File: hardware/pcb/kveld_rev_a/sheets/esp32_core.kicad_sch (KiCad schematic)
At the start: 0 parts

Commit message: feat(hw): capture rev a schematic and refine enclosure
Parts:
- added C27: 1uF, Capacitor_SMD:C_0603_1608Metric, symbol Device:C
- added C28: 100nF, Capacitor_SMD:C_0603_1608Metric, symbol Device:C
- added C29: 10uF, Capacitor_SMD:C_0603_1608Metric, symbol Device:C
- added C30: 47uF, Capacitor_SMD:C_0805_2012Metric, symbol Device:C
- added R25, R26: 10k, Resistor_SMD:R_0603_1608Metric, symbol Device:R
- added U1: ESP32-S3-WROOM-1-N16 / WROOM-1U-N16, RF_Module:ESP32-S3-WROOM-1, symbol RF_Module:ESP32-S3-WROOM-1
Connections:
- new net 3V3: C28.1, C29.1, C30.1, R25.1, R26.1, U1.2 (3V3)
- new net BOOT_IO0: R26.2, U1.27 (IO0)
- new net BTN_CATEGORY: U1.4 (IO4)
- new net BTN_NEXT: U1.10 (IO17)
- new net CHG_ENABLE: U1.22 (IO14)
- new net CHG_STAT1: U1.6 (IO6)
- new net CHG_STAT2: U1.7 (IO7)
- new net CHIP_EN: C27.1, R25.2, U1.3 (EN)
- new net EPD_BUSY: U1.17 (IO9)
- new net EPD_CLK: U1.20 (IO12)
- new net EPD_CS: U1.18 (IO10)
- new net EPD_DC: U1.11 (IO18)
- new net EPD_MOSI: U1.19 (IO11)
- new net EPD_PWR_EN: U1.5 (IO5)
- new net EPD_RESET: U1.12 (IO8)
- new net FACTORY_RESET_OD: U1.31 (IO38)
- new net GND: C27.2, C28.2, C29.2, C30.2, U1.1 (GND), U1.40 (GND), U1.41 (GND)
- new net STATUS_GREEN: U1.9 (IO16)
- new net STATUS_RED: U1.8 (IO15)
- new net UART0_RX: U1.36 (RXD0)
- new net UART0_TX: U1.37 (TXD0)
- new net USB_DN: U1.13 (USB_D-)
- new net USB_DP: U1.14 (USB_D+)
- new net VBAT_SENSE: U1.39 (IO1)
- new net VBAT_SENSE_EN: U1.38 (IO2)
- new net VBUS_SENSE: U1.23 (IO21)
- no-connect marks 0 -> 13
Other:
- note added: "Preferred assembly: WROOM-1-N16. WROOM-1U-N16 stays open as the placement/RF fallback."
- title: (none) -> ESP32-S3 module core

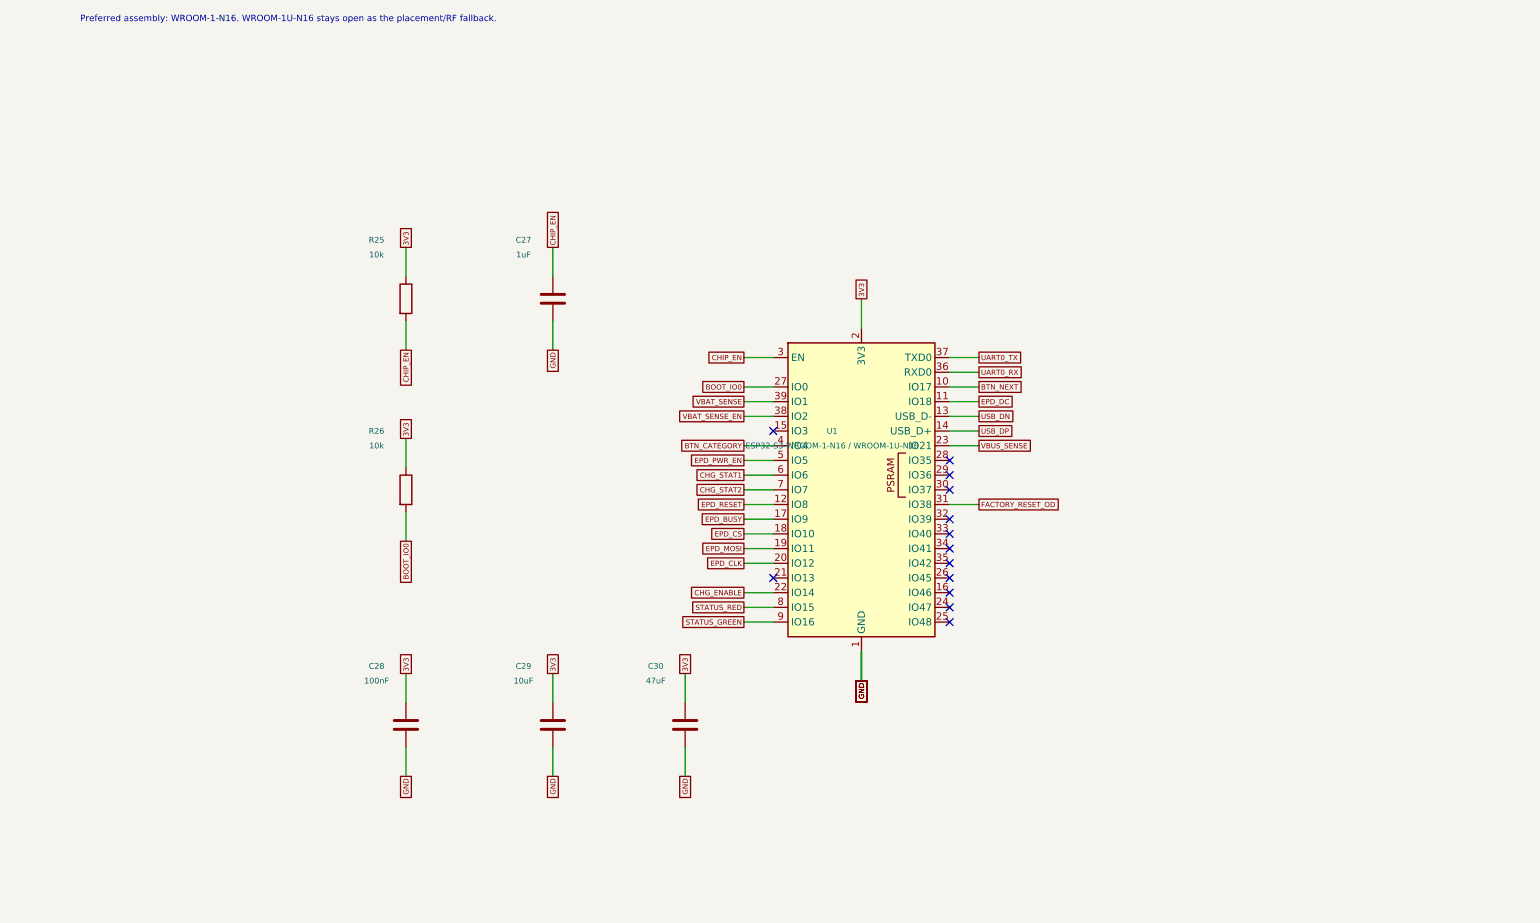
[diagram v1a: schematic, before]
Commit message: refactor(hw): consolidate and clarify schematic
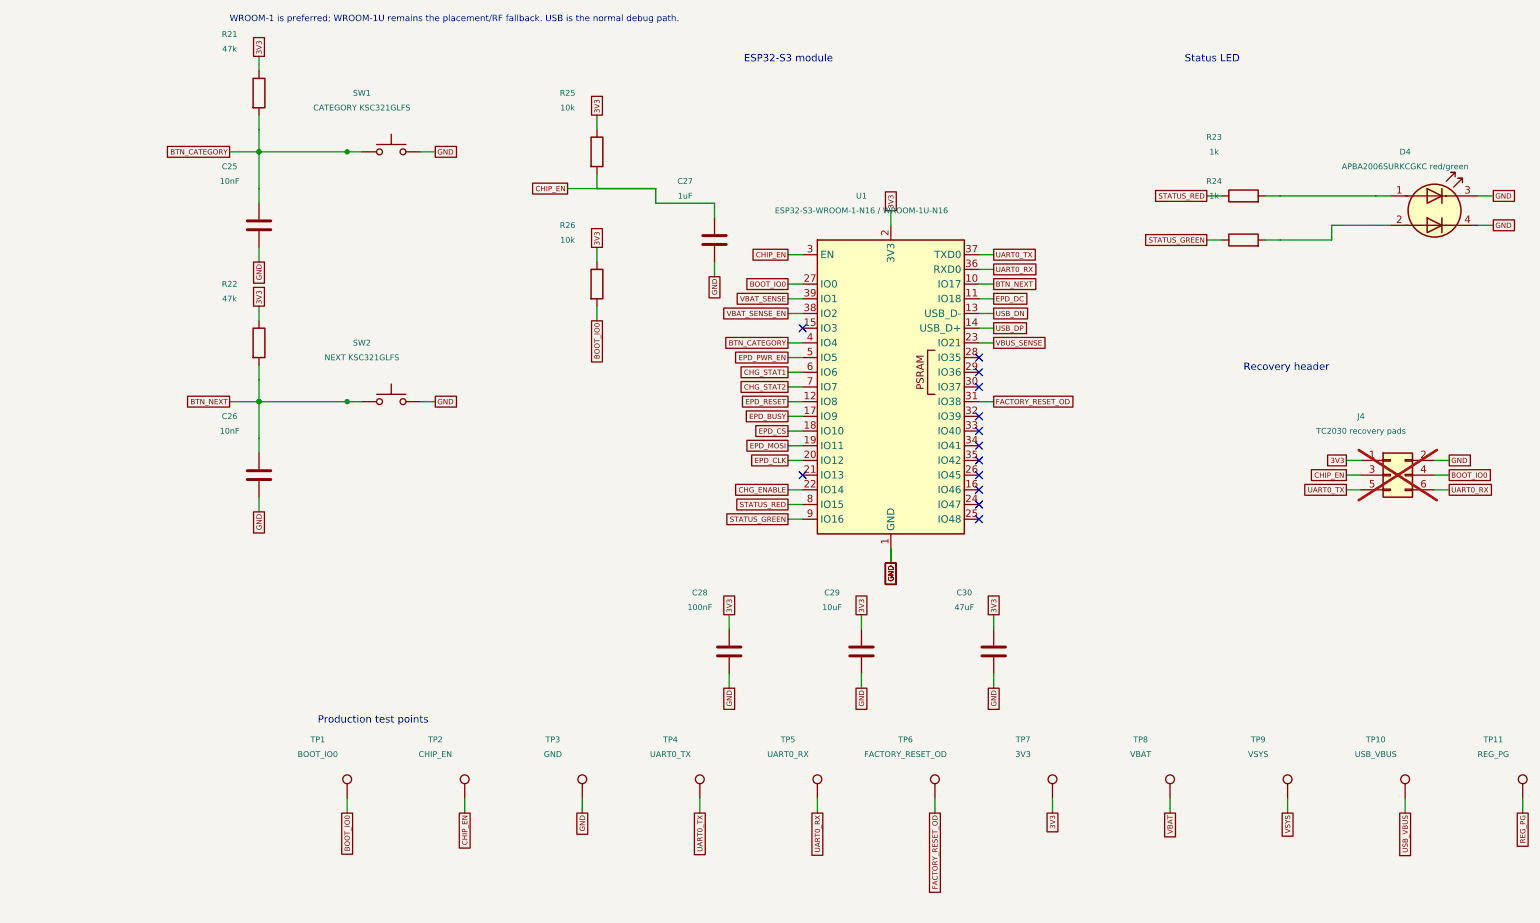
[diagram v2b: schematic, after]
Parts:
- added C25, C26: 10nF, Capacitor_SMD:C_0603_1608Metric, symbol Device:C
- added D4: APBA2006SURKCGKC red/green, symbol Device:LED_Dual_AAKK
- added J4: TC2030 recovery pads, Connector:Tag-Connect_TC2030-IDC-NL_2x03_P1.27mm_Vertical, symbol Connector_Generic:Conn_02x03_Odd_Even
- added R21, R22: 47k, Resistor_SMD:R_0603_1608Metric, symbol Device:R
- added R23, R24: 1k, Resistor_SMD:R_0603_1608Metric, symbol Device:R
- added SW1: CATEGORY KSC321GLFS, symbol Switch:SW_Push
- added SW2: NEXT KSC321GLFS, symbol Switch:SW_Push
- added TP1: BOOT_IO0, TestPoint:TestPoint_Pad_D1.0mm, symbol Connector:TestPoint
- added TP10: USB_VBUS, TestPoint:TestPoint_Pad_D1.0mm, symbol Connector:TestPoint
- added TP11: REG_PG, TestPoint:TestPoint_Pad_D1.0mm, symbol Connector:TestPoint
- added TP2: CHIP_EN, TestPoint:TestPoint_Pad_D1.0mm, symbol Connector:TestPoint
- added TP3: GND, TestPoint:TestPoint_Pad_D1.0mm, symbol Connector:TestPoint
- added TP4: UART0_TX, TestPoint:TestPoint_Pad_D1.0mm, symbol Connector:TestPoint
- added TP5: UART0_RX, TestPoint:TestPoint_Pad_D1.0mm, symbol Connector:TestPoint
- added TP6: FACTORY_RESET_OD, TestPoint:TestPoint_Pad_D1.0mm, symbol Connector:TestPoint
- added TP7: 3V3, TestPoint:TestPoint_Pad_D1.0mm, symbol Connector:TestPoint
- added TP8: VBAT, TestPoint:TestPoint_Pad_D1.0mm, symbol Connector:TestPoint
- added TP9: VSYS, TestPoint:TestPoint_Pad_D1.0mm, symbol Connector:TestPoint
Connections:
- net 3V3: now also J4.1 (Pin_1), R21.1, R22.1, TP7.1
- net BOOT_IO0: now also J4.4 (Pin_4), TP1.1
- net BTN_CATEGORY: now also C25.1, R21.2, SW1.1
- net BTN_NEXT: now also C26.1, R22.2, SW2.1
- net CHIP_EN: now also J4.3 (Pin_3), TP2.1
- net FACTORY_RESET_OD: now also TP6.1
- net GND: now also C25.2, C26.2, D4.3 (K1), D4.4 (K2), J4.2 (Pin_2), SW1.2, SW2.2, TP3.1
- net STATUS_GREEN: now also R24.1
- net STATUS_RED: now also R23.1
- net UART0_RX: now also J4.6 (Pin_6), TP5.1
- net UART0_TX: now also J4.5 (Pin_5), TP4.1
- new net: D4.2 (A2), R24.2
- new net: D4.1 (A1), R23.2
- new net REG_PG: TP11.1
- new net USB_VBUS: TP10.1
- new net VBAT: TP8.1
- new net VSYS: TP9.1
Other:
- note added: "ESP32-S3 module"
- note added: "Production test points"
- note added: "Recovery header"
- note added: "Status LED"
- note added: "WROOM-1 is preferred; WROOM-1U remains the placement/RF fallback. USB is the normal debug path."
- note removed: "Preferred assembly: WROOM-1-N16. WROOM-1U-N16 stays open as the placement/RF fallback."
- title: ESP32-S3 module core -> Controller, user I/O, and recovery

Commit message: fix(hw): use native ground symbols
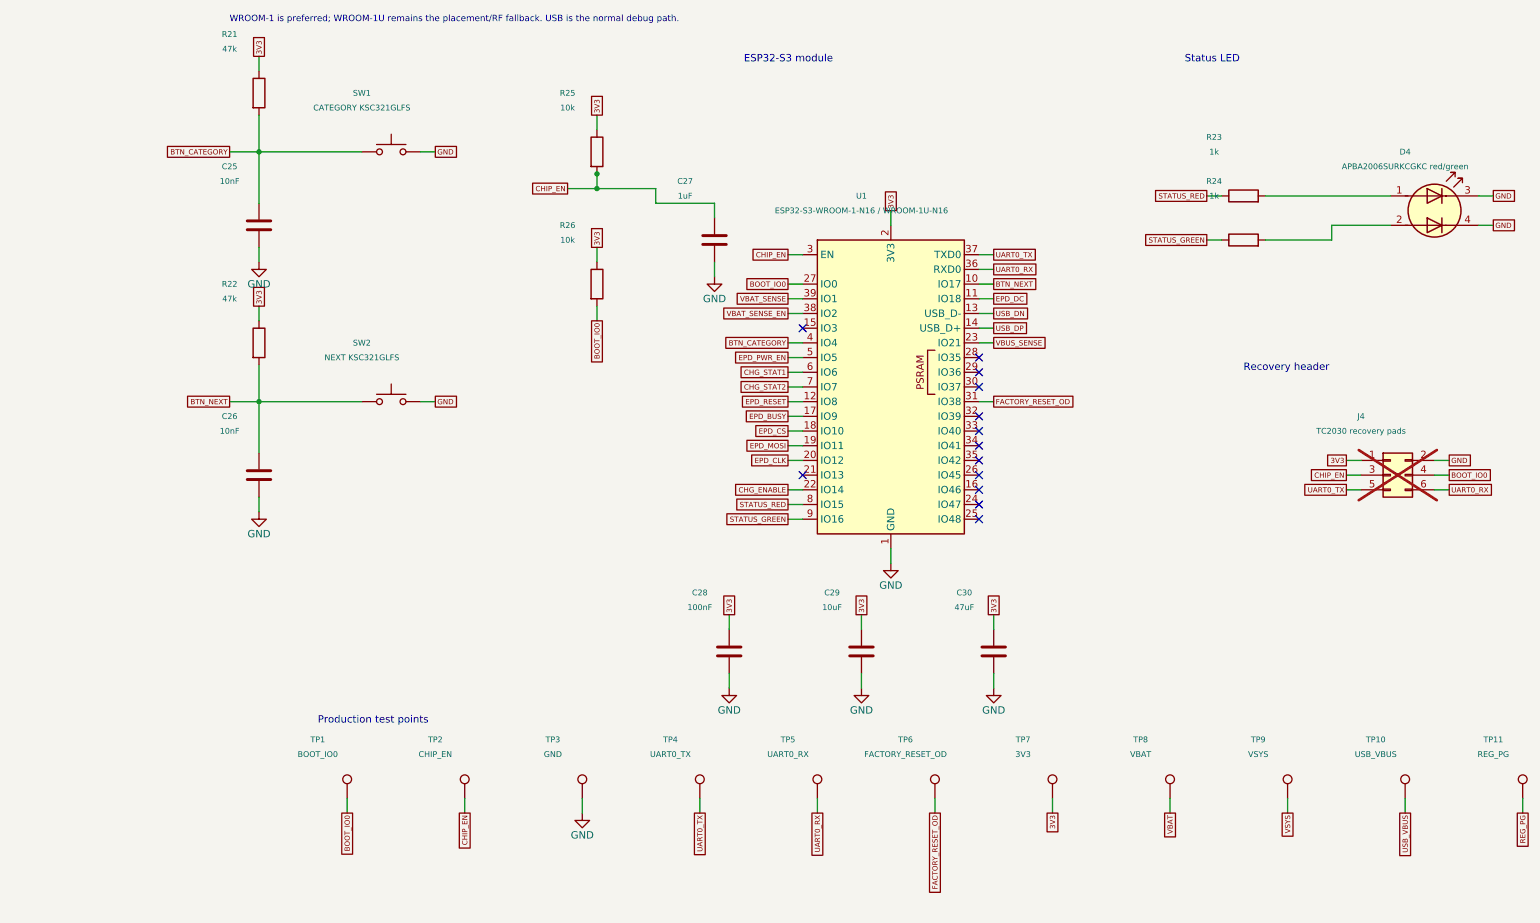
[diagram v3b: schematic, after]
